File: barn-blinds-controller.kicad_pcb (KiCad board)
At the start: 4 copper layers, 65 x 60 mm, 73 parts, among them J1 DC005-T25, J2 KH-TYPE-C-16P (Kinghelm), J3 Conn_01x08, SW1 RESET, SW2 BOOT, U1 DCDC Converter, U10 TMP235, U11 ACS723xLCTR-05AB, U2 AP2112K-3.3, U3 ESP32-S3-WROOM-1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

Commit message: Sent for production
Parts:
- J3: footprint barn_shade_controller:TerminalBlock_JL271R-35008G01_Spring_1x08_P3.50mm_Horizontal -> barn_shade_controller:CONN-TH_8P-P3.50_JL271R-35008G01
- moved J3 12.6 mm to (135.3, 76.2)
- moved D4 2.58 mm to (131.5, 56.1), turned to 90 degrees
- moved F1 2.00 mm to (137.0, 58.6)
- moved D6 0.44 mm to (135.4, 64.9)
- moved D7 0.44 mm to (135.4, 79.5)
- moved F2 0.44 mm to (135.4, 86.8)
- moved F3 0.44 mm to (135.4, 71.9)
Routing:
- net Net-(D5-Pad2): track 21.0 -> 27.2 mm
- net Net-(D7-Pad2): track 38.0 -> 44.0 mm
- net U2_A02: track 20.9 -> 23.7 mm
- net U2_A01: track 32.8 -> 30.3 mm, vias 2 -> 1
- net U3_B02: track 28.7 -> 31.1 mm
- net U2_B01: track 9.41 -> 11.7 mm
- net U2_B02: track 31.8 -> 33.9 mm
- net Net-(D4-Pad2): track 30.7 -> 32.6 mm
- net U3_A02: track 24.4 -> 25.9 mm
- net /GPIO14: track 18.4 -> 17.0 mm
- net U3_B01: track 11.9 -> 13.0 mm
- net +5V_OR: track 23.0 -> 22.4 mm
- net +3.3V_MOTOR: track 39.4 -> 39.8 mm, vias 10 -> 9
- net +12V: vias 14 -> 10
- net GND_MOTOR: vias 36 -> 34

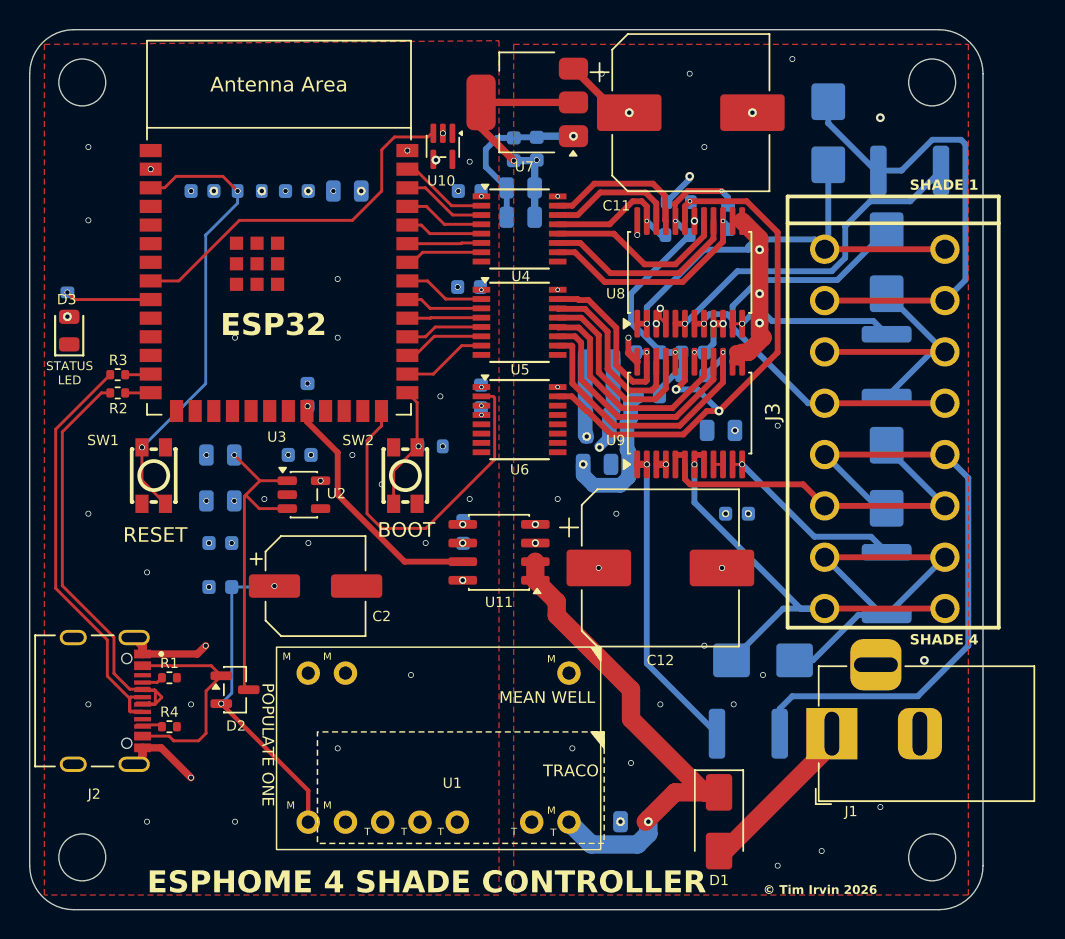
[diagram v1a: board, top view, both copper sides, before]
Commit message: Refactored board to use larger vias and route better paths.
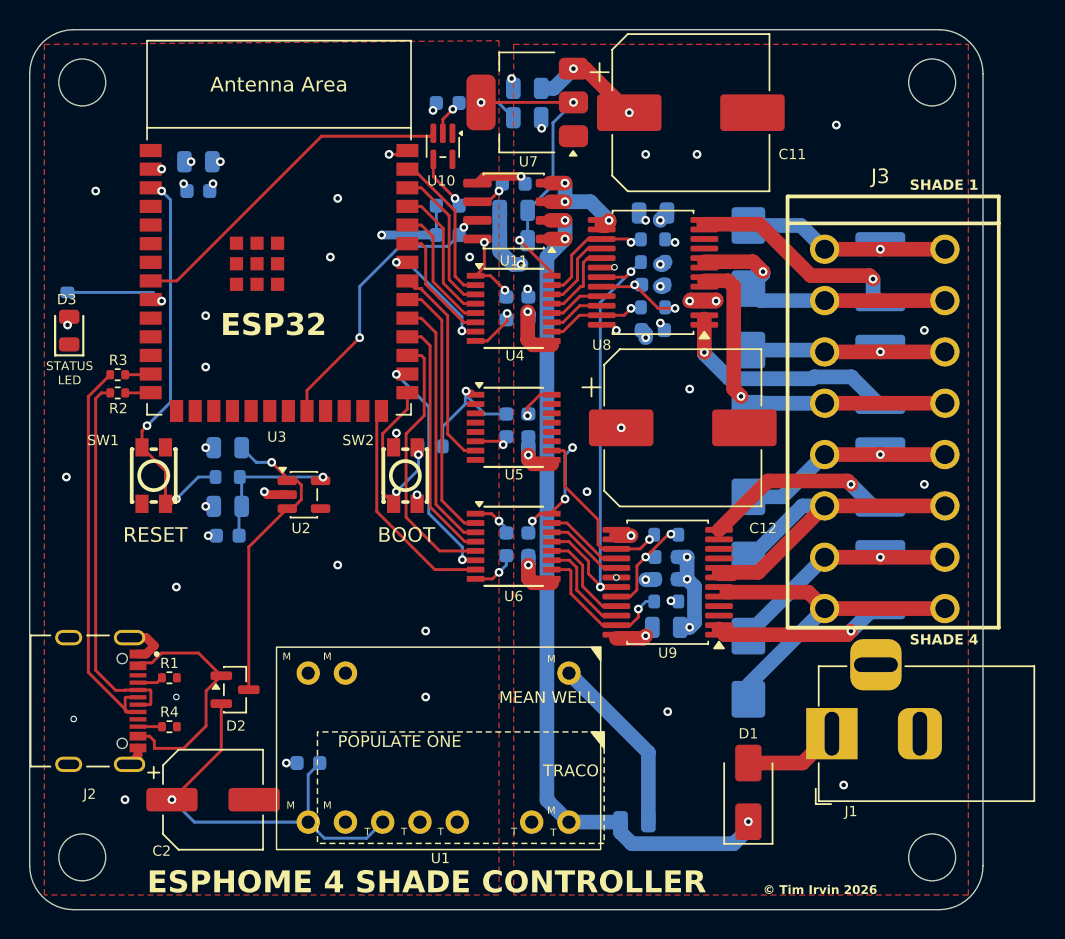
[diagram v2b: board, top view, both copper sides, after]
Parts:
- moved C9 26.1 mm to (110.9, 53.0)
- moved C_TMP1 26.0 mm to (105.5, 54.0), turned to 0 degrees
- moved C10 25.1 mm to (110.9, 55.0)
- moved C_ISO_E1 24.2 mm to (109.5, 84.1), turned to 90 degrees
- moved C_FILT1 24.0 mm to (110.0, 59.5), turned to 0 degrees
- moved U11 23.3 mm to (110.0, 61.4)
- moved F3 19.7 mm to (135.0, 79.5), turned to -90 degrees
- moved R5 19.6 mm to (90.5, 79.5)
- moved C_ISO_D1 18.9 mm to (111.0, 76.0), turned to -90 degrees
- moved R8 17.0 mm to (120.4, 88.0)
- moved C_VM_A2 16.9 mm to (120.4, 89.8), turned to 0 degrees
- moved C_ACS1 16.7 mm to (105.5, 61.0)
- moved C2 16.2 mm to (89.5, 101.5)
- moved C_ACS2 14.5 mm to (105.5, 63.0), turned to 180 degrees
- moved C_ISO_F1 14.4 mm to (111.0, 84.1), turned to -90 degrees
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- renumbered D6 to D5, D7 to D6, D5 to D7, F3 to F2, F4 to F3, F2 to F4
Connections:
- C10 pad 1: unconnected-(C10-Pad1) -> +3.3V_MOTOR
- C9 pad 1: unconnected-(C9-Pad1) -> +12V
- D4 pad 1: U2_A01 -> Net-(D4-Pad1)
- D4 pad 2: Net-(D4-Pad2) -> U2_B02
- D5 pad 1: U2_B02 -> U2_A02
- D6 pad 1: U3_A02 -> U3_B02
- D7 pad 1: U3_B02 -> U3_A02
- F1 pad 1: U2_A02 -> U2_B01
- F1 pad 2: Net-(D4-Pad2) -> Net-(D4-Pad1)
- F2 pad 1: U2_B01 -> U2_A01
- F3 pad 2: U3_A01 -> U3_B01
- F4 pad 1: U3_B01 -> U3_A01
- J3 pad 1: U3_B02 -> U3_A02
- J3 pad 3: U3_A02 -> U3_B02
- J3 pad 5: U2_B02 -> U2_A02
- J3 pad 7: Net-(D4-Pad2) -> U2_B02
- J3 pad 8: U2_A01 -> Net-(D4-Pad1)
- U3 pad 26: /ISO_STBY -> /ISO_PWM_M3
- U3 pad 28: /ISO_PWM_M4 -> /ISO_M3_CLOSE
- U3 pad 29: /ISO_M4_CLOSE -> /ISO_M3_OPEN
- U3 pad 30: /ISO_M4_OPEN -> /ISO_STBY
- U3 pad 31: /ISO_M3_OPEN -> /ISO_M4_OPEN
- U3 pad 32: /ISO_M3_CLOSE -> /ISO_M4_CLOSE
- U3 pad 33: /ISO_PWM_M3 -> /ISO_PWM_M4
- U3 pad 34: /ISO_PWM_M2 -> /ISO_PWM_M1
- U3 pad 35: /ISO_M2_CLOSE -> /ISO_M1_CLOSE
- U3 pad 36: /ISO_M2_OPEN -> /ISO_M1_OPEN
- U3 pad 37: /ISO_PWM_M1 -> /ISO_M2_OPEN
- U3 pad 38: /ISO_M1_CLOSE -> /ISO_M2_CLOSE
- U3 pad 39: /ISO_M1_OPEN -> /ISO_PWM_M2
- U4 pad 10: /PWM_M2 -> /PWM_M1
- U4 pad 11: /M2_BIN2 -> /M1_AIN2
- U4 pad 12: /M2_BIN1 -> /M1_AIN1
- U4 pad 13: /PWM_M1 -> /M2_BIN1
- U4 pad 14: /M1_AIN2 -> /M2_BIN2
- U4 pad 15: /M1_AIN1 -> /PWM_M2
- U4 pad 2: /ISO_M1_OPEN -> /ISO_PWM_M2
- U4 pad 3: /ISO_M1_CLOSE -> /ISO_M2_CLOSE
- U4 pad 4: /ISO_PWM_M1 -> /ISO_M2_OPEN
- U4 pad 5: /ISO_M2_OPEN -> /ISO_M1_OPEN
- U4 pad 6: /ISO_M2_CLOSE -> /ISO_M1_CLOSE
- U4 pad 7: /ISO_PWM_M2 -> /ISO_PWM_M1
- U5 pad 11: /M4_BIN2 -> unconnected-(U5-OUTE-Pad11)
- U5 pad 12: /M4_BIN1 -> unconnected-(U5-OUTD-Pad12)
- U5 pad 13: /M3_AIN1 -> unconnected-(U5-OUTC-Pad13)
- U5 pad 14: /M3_AIN2 -> unconnected-(U5-OUTB-Pad14)
- U5 pad 15: /PWM_M3 -> unconnected-(U5-OUTA-Pad15)
- U5 pad 2: /ISO_PWM_M3 -> GND_ISO
- U5 pad 3: /ISO_M3_CLOSE -> GND_ISO
- U5 pad 4: /ISO_M3_OPEN -> GND_ISO
- U5 pad 5: /ISO_M4_OPEN -> GND_ISO
- U5 pad 6: /ISO_M4_CLOSE -> GND_ISO
- U6 pad 10: unconnected-(U6-OUTF-Pad10) -> /PWM_M3
- U6 pad 11: unconnected-(U6-OUTE-Pad11) -> /M3_AIN2
- U6 pad 12: unconnected-(U6-OUTD-Pad12) -> /M3_AIN1
- U6 pad 13: unconnected-(U6-OUTC-Pad13) -> /STBY
- U6 pad 14: unconnected-(U6-OUTB-Pad14) -> /M4_BIN1
- U6 pad 15: /STBY -> /M4_BIN2
- U6 pad 2: /ISO_STBY -> /ISO_M4_CLOSE
- U6 pad 3: GND_ISO -> /ISO_M4_OPEN
- U6 pad 4: GND_ISO -> /ISO_STBY
- U6 pad 5: GND_ISO -> /ISO_M3_OPEN
- U6 pad 6: GND_ISO -> /ISO_M3_CLOSE
- U6 pad 7: GND_ISO -> /ISO_PWM_M3
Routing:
- net Net-(D4-Pad2): track 32.6 -> 0.00 mm
- net +3.3V_ISO: track 0.00 -> 30.7 mm, vias 15 -> 10
- net Net-(D6-Pad2): track 44.0 -> 15.2 mm, vias 0 -> 1
- net +12V_RAW: track 33.5 -> 58.4 mm, vias 1 -> 3
- net GND_ISO: track 11.4 -> 30.7 mm, vias 39 -> 30
- net Net-(D4-Pad1): track 0.00 -> 14.7 mm, vias 0 -> 1
- net U2_A01: track 30.3 -> 16.0 mm
- net U2_B02: track 33.9 -> 19.6 mm
- net /ISO_M3_OPEN: track 5.06 -> 18.3 mm
- net /ISO_M4_CLOSE: track 5.59 -> 18.2 mm
- net /ISO_M4_OPEN: track 5.33 -> 17.6 mm
- net /M4_BIN2: track 16.7 -> 5.00 mm
- net /ISO_M3_CLOSE: track 5.30 -> 16.2 mm, vias 0 -> 2
- net Net-(D7-Pad2): track 27.2 -> 16.3 mm, vias 0 -> 1
- net /M4_BIN1: track 15.7 -> 5.01 mm
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
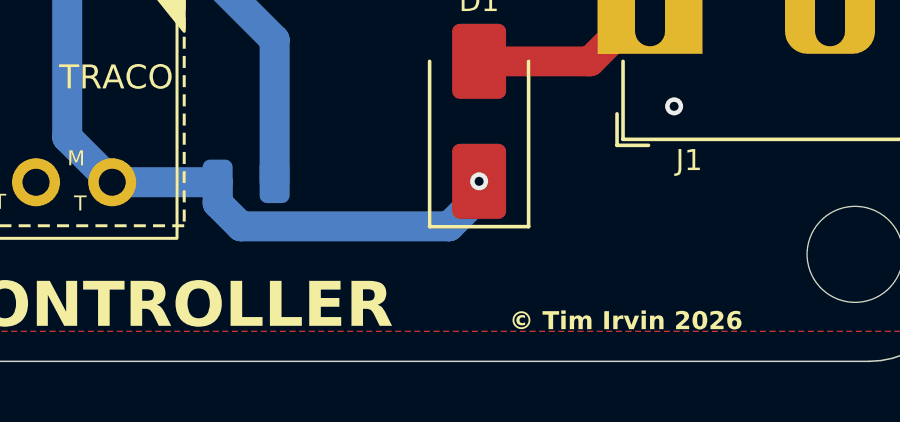
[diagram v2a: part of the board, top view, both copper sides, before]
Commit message: Added revision text to board
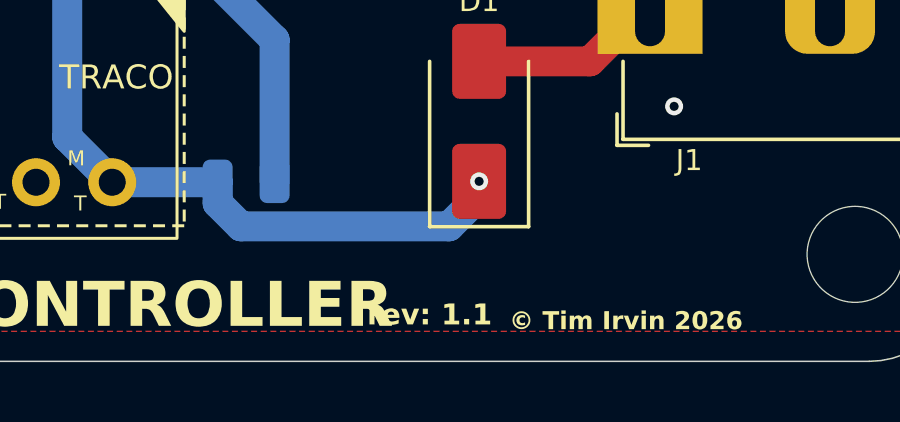
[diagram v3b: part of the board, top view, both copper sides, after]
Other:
- board text added: "rev: 1.1"
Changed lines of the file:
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@@
+		)
+	)
+	(gr_text "rev: 1.1"
+		(at 122.264269 107.854095 0)
+		(layer "F.SilkS")
+		(effects
+			(font
+				(size 0.7 0.7)
+				(thickness 0.14)
+				(bold yes)
+			)
+			(justify left bottom)
 		)
 	)

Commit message: V 1.2
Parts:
- added D8: White, PCM_JLCPCB:D_0805, F.Cu at (79.5, 58.6)
- added D9: Blue, Diode_SMD:D_0805_2012Metric, F.Cu at (131.5, 55.1)
- added J4: Conn_01x05, Connector_PinHeader_2.54mm:PinHeader_1x05_P2.54mm_Vertical, F.Cu at (79.5, 75.4)
- added R_LED2: 1K, Resistor_SMD:R_0603_1608Metric, B.Cu at (80.0, 57.5)
- added R_LED3: 1.8K, Resistor_SMD:R_0603_1608Metric, B.Cu at (130.5, 54.0)
- added TP1: 3.3V_ISO, barn_shade_controller:TestPoint_Pad_D1.0mm_No_SolderMask, F.Cu at (104.0, 88.5)
- added TP2: EN, barn_shade_controller:TestPoint_Pad_D1.0mm_No_SolderMask, F.Cu at (92.0, 88.5)
- added TP3: GPIO0, barn_shade_controller:TestPoint_Pad_D1.0mm_No_SolderMask, F.Cu at (101.0, 88.5)
- added TP4: ASC Out, barn_shade_controller:TestPoint_Pad_D1.0mm_No_SolderMask, F.Cu at (95.0, 88.5)
- added TP5: STBY, barn_shade_controller:TestPoint_Pad_D1.0mm_No_SolderMask, F.Cu at (115.0, 59.5)
- added TP7: 12V, barn_shade_controller:TestPoint_Pad_D1.0mm_No_SolderMask, F.Cu at (122.0, 99.5)
- added TP8: 5V_ISO, barn_shade_controller:TestPoint_Pad_D1.0mm_No_SolderMask, F.Cu at (98.0, 88.5)
- D2: value BAT54S -> BAT54C; moved to B.Cu
- J1: value DC005-T25 -> DC005-T20
- U2: moved to B.Cu
- moved R5 19.6 mm to (88.5, 60.0)
- moved U1 7.21 mm to (107.1, 100.4)
- moved C3 6.96 mm to (89.5, 101.5), turned to 0 degrees
- moved C_VM_A2 6.96 mm to (118.0, 83.2)
- moved R10 5.54 mm to (114.0, 65.5), turned to 90 degrees
- moved D2 5.39 mm to (86.0, 96.0)
- moved C1 5.34 mm to (113.5, 105.4), turned to 180 degrees
- moved C_VM_B2 4.69 mm to (118.0, 90.5)
- moved C8 4.03 mm to (92.5, 57.5)
- moved C7 4.01 mm to (92.5, 59.4)
- moved C_ACS1 3.56 mm to (104.9, 57.5), turned to 90 degrees
- moved R_BOOT1 3.37 mm to (101.0, 77.5), turned to 180 degrees
- moved C_VCC_B2 3.15 mm to (118.0, 87.0), turned to 180 degrees
- moved R9 3.00 mm to (118.0, 85.2)
- moved R8 2.52 mm to (118.0, 88.7)
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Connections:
- C_ACS2 pad 1: /GPIO14 -> /ACS723
- R2 pad 2: /GPIO20 -> /USB_DN
- R3 pad 2: /GPIO19 -> /USB_DP
- R_BOOT1 pad 1: Net-(U3-GPIO0/BOOT) -> Net-(J4-Pin_5)
- SW1 pad 1: GND_ISO -> Net-(U3-EN)
- SW1 pad 4: Net-(U3-EN) -> GND_ISO
- SW2 pad 1: Net-(U3-GPIO0/BOOT) -> Net-(J4-Pin_5)
- SW2 pad 2: GND_ISO -> Net-(J4-Pin_5)
- SW2 pad 3: Net-(U3-GPIO0/BOOT) -> GND_ISO
- U10 pad 3: /GPIO15 -> /TMP235
- U11 pad 7: /GPIO14 -> /ACS723
- U3 pad 10: unconnected-(U3-GPIO17/U1TXD/ADC2_CH6-Pad10) -> Net-(J4-Pin_1)
- U3 pad 11: unconnected-(U3-GPIO18/U1RXD/ADC2_CH7/CLK_OUT3-Pad11) -> Net-(J4-Pin_2)
- U3 pad 13: /GPIO19 -> /USB_DN
- U3 pad 14: /GPIO20 -> /USB_DP
- U3 pad 18: unconnected-(U3-GPIO10/TOUCH10/ADC1_CH9/FSPICS0/FSPIIO4/SUBSPICS0-Pad18) -> /ACS723
- U3 pad 22: /GPIO14 -> unconnected-(U3-GPIO14/TOUCH14/ADC2_CH3/FSPIWP/FSPIDQS/SUBSPIWP-Pad22)
- U3 pad 27: Net-(U3-GPIO0/BOOT) -> Net-(J4-Pin_5)
- U3 pad 7: unconnected-(U3-GPIO7/TOUCH7/ADC1_CH6-Pad7) -> /TMP235
- U3 pad 8: /GPIO15 -> unconnected-(U3-GPIO15/U0RTS/ADC2_CH4/XTAL_32K_P-Pad8)
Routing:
- net +12V_RAW: track 58.4 -> 1.94 mm, vias 3 -> 4
- net +3.3V_MOTOR: track 49.4 -> 8.16 mm, vias 14 -> 7
- net Net-(J4-Pin_5): track 0.00 -> 38.5 mm, vias 0 -> 4
- net /ACS723: track 0.00 -> 37.1 mm, vias 0 -> 2
- net GND_MOTOR: track 37.9 -> 7.18 mm, vias 26 -> 23
- net +5V_ISO: track 28.2 -> 0.00 mm, vias 1 -> 4
- net /GPIO15: track 23.4 -> 0.00 mm
- net /TMP235: track 0.00 -> 23.2 mm, vias 0 -> 2
- net /GPIO14: track 20.0 -> 0.00 mm, vias 2 -> 0
- net +12V: track 19.8 -> 0.00 mm, vias 12 -> 11
- net +3.3V_ISO: track 30.7 -> 13.4 mm, vias 10 -> 12
- net GND_ISO: track 30.7 -> 15.3 mm, vias 30 -> 27
- net Net-(U3-GPIO0/BOOT): track 13.2 -> 0.00 mm, vias 2 -> 0
- net Net-(J4-Pin_2): track 0.00 -> 10.7 mm, vias 0 -> 1
- net VBUS: track 16.4 -> 6.86 mm, vias 0 -> 2
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- added copper zone on In2.Cu, net +12V_RAW
- added copper zone on B.Cu, net +3.3V_ISO
- added copper zone on B.Cu, net +3.3V_MOTOR
- added copper zone on B.Cu, net +5V_ISO
- added copper zone on In2.Cu, net +5V_ISO
- added copper zone on B.Cu, net GND_MOTOR
- removed copper zone on In2.Cu, net +3.3V_MOTOR
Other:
- board text added: "12V POWER"
- board text added: "3.3V"
- board text added: "ESP32 POWER"
- board text added: "GND"
- board text added: "GPIO0"
- board text added: "RX"
- board text added: "TX"
- board text added: "VSP-WSC-4"
- board text added: "WINDOW SHADE CONTROLLER • 4"
- board text added: "rev: 1.2"
- board text added: "© Vesprio.io 2026"
- board text removed: "ESPHOME 4 SHADE CONTROLLER"
- board text removed: "rev: 1.1"
- board text removed: "© Tim Irvin 2026"
